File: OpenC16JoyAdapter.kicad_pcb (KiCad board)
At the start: 2 copper layers, 30.5 x 33 mm, 13 parts, among them J1 DB9 Male, P1 CONN_01X08, P2 CONN_01X02, U1 74LS244

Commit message: Refined board a bit
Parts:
- removed G***: LOGO, w_logo:Logo_copper_OSHW_6x6mm
- added P3: OSHW_LOGO_PLACEHOLDER, w_logo:Logo_copper_OSHW_6x6mm, B.Cu at (157.2, 109.0)
- C1: footprint smd_cap:c_0805 -> Capacitors_SMD:C_0805_HandSoldering
- D1: footprint LEDs:LED_0805 -> LEDs:LED_0805_HandSoldering
- P1: value CONN_01X08 -> TO_C16_MINI_DIN_8
- P2: value CONN_01X02 -> PIN5_POWER
- turned C1 to 270 degrees
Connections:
- net /DOWN renamed /c16_down
- net /FIRE renamed /c16_fire
- net /LEFT renamed /c16_left
- net /RIGHT renamed /c16_right
- net /SEL renamed /c16_select
- net /UP renamed /c16_up
- net Net-(J1-Pad1) renamed /md_up
- net Net-(J1-Pad2) renamed /md_down
- net Net-(J1-Pad3) renamed /md_left
- net Net-(J1-Pad4) renamed /md_right
- net Net-(J1-Pad6) renamed /md_b_~a
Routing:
- net GND: track 47.8 -> 56.9 mm, vias 2 -> 3
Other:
- board text added: "github.com/SukkoPera/OpenC16JoyAdapter"
- board text removed: "https://github.com/SukkoPera/"

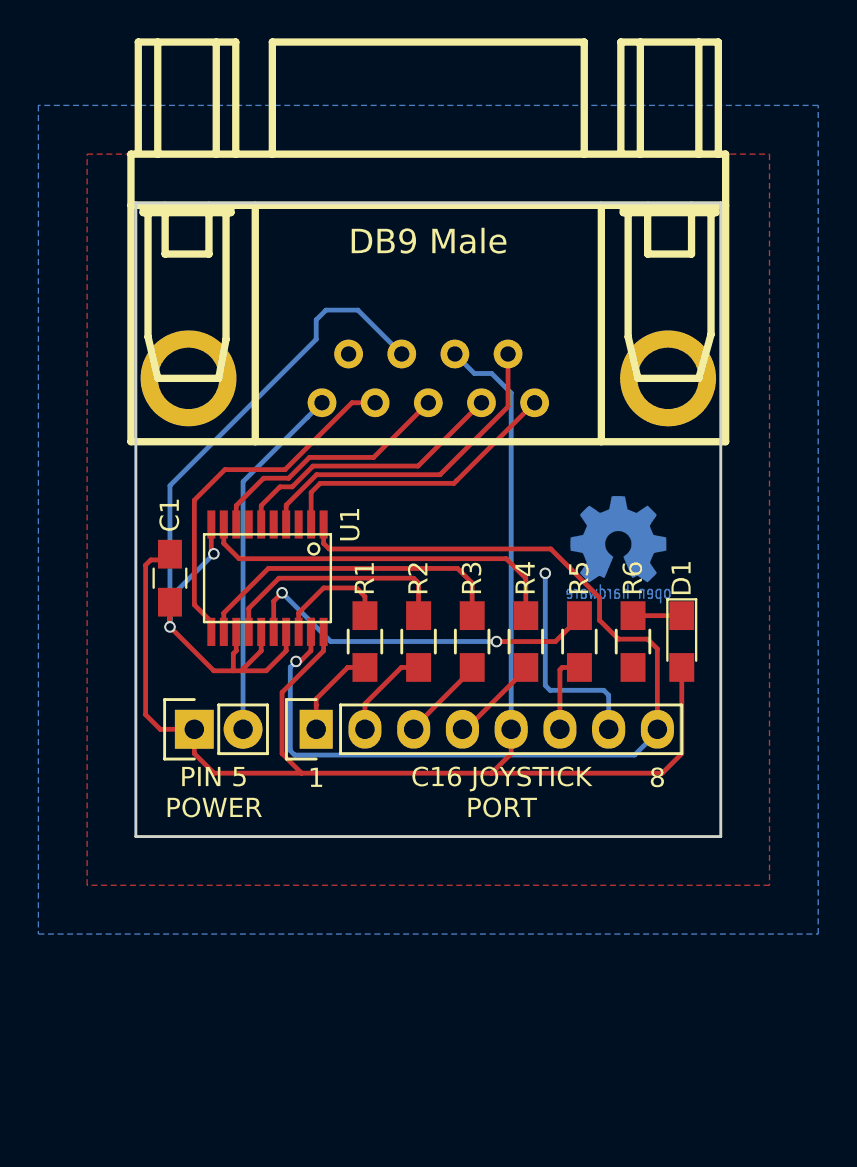
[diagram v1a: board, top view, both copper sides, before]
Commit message: Smooth lower corners, stitch ground planes, fix 3D models, add version no.
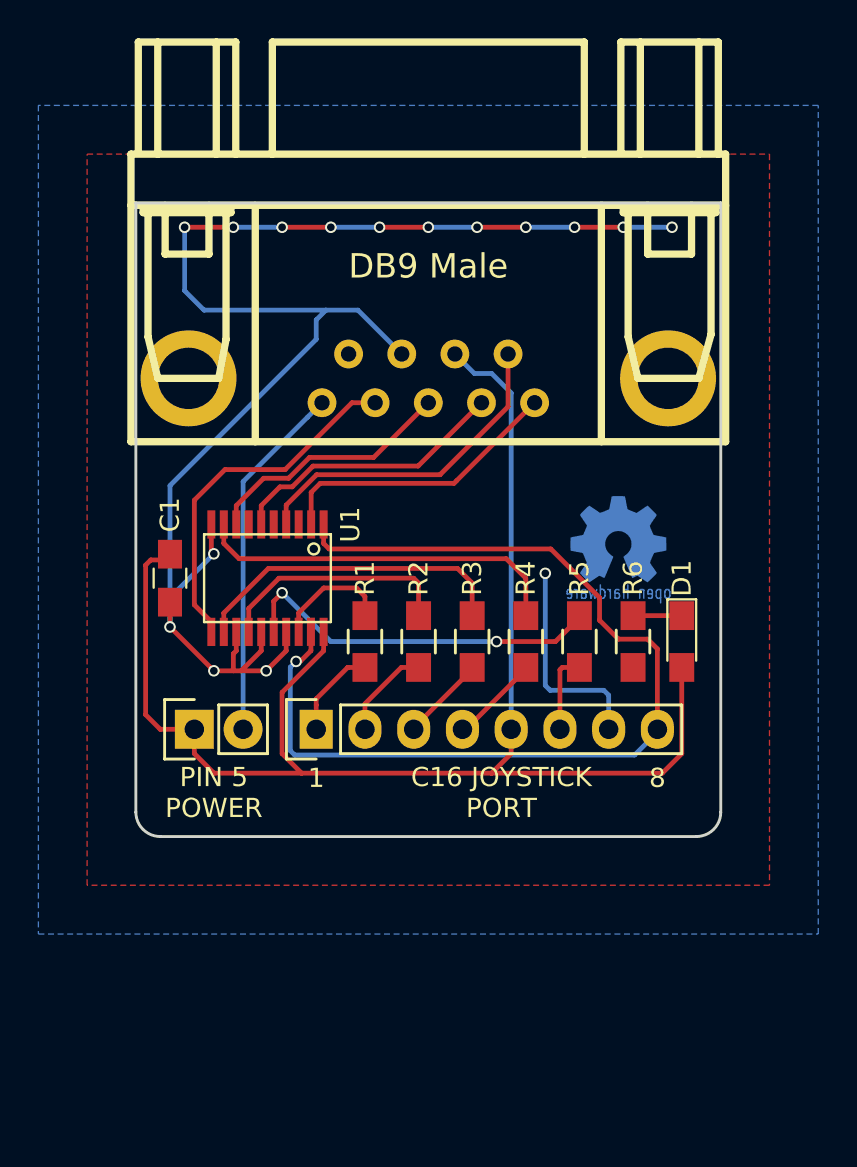
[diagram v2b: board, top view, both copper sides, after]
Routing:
- net GND: track 56.9 -> 93.4 mm, vias 3 -> 16
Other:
- outline, holes or cut-outs redrawn
- board text added: "V2"
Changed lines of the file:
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@@
 (kicad_pcb (version 4) (host pcbnew 4.0.7)
   (general
-    (links 31)
+    (links 0)
     (no_connects 0)
     (area 132.004999 91.364999 162.635001 124.535001)
     (thickness 1.6)
-    (drawings 11)
-    (tracks 159)
+    (drawings 14)
+    (tracks 185)
     (zones 0)
     (modules 13)
@@
       (effects (font (thickness 0.3048)))
     )
-    (fp_text value "DB9 Male" (at 0 0 180) (layer F.SilkS)
+    (fp_text value "DB9 Male" (at 0 -1.27 180) (layer F.SilkS)
       (effects (font (thickness 0.3048)))
     )
@@
     (pad 8 thru_hole oval (at 0 17.78 90) (size 2.032 1.7272) (drill 1.016) (layers *.Cu *.Mask)
       (net 20 /c16_select))
-    (model Pin_Headers.3dshapes/Pin_Header_Straight_1x08.wrl
-      (at (xyz 0 -0.35 0))
-      (scale (xyz 1 1 1))
-      (rotate (xyz 0 0 90))
+    (model Pin_Headers.3dshapes/Pin_Header_Straight_1x08_Pitch2.54mm.wrl
+      (at (xyz 0 0 0))
+      (scale (xyz 1 1 1))
+      (rotate (xyz 0 0 0))
     )
   )
@@
     (pad 2 thru_hole oval (at 0 2.54 90) (size 2.032 2.032) (drill 1.016) (layers *.Cu *.Mask)
       (net 8 "Net-(J1-Pad5)"))
-    (model Pin_Headers.3dshapes/Pin_Header_Straight_1x02.wrl
-      (at (xyz 0 -0.05 0))
-      (scale (xyz 1 1 1))
-      (rotate (xyz 0 0 90))
+    (model Pin_Headers.3dshapes/Pin_Header_Straight_1x02_Pitch2.54mm.wrl
+      (at (xyz 0 0 0))
+      (scale (xyz 1 1 1))
+      (rotate (xyz 0 0 0))
     )
   )
@@
       (xy -1.51384 -2.24536)) (layer B.Cu) (width 0.00254))
   )
+  (gr_text V2 (at 134.62 94.488) (layer B.SilkS)
+    (effects (font (size 1.5 1.5) (thickness 0.3)) (justify mirror))
+  )
+  (gr_arc (start 161.29 123.19) (end 162.56 123.19) (angle 90) (layer Edge.Cuts) (width 0.15))
+  (gr_arc (start 133.35 123.19) (end 133.35 124.46) (angle 90) (layer Edge.Cuts) (width 0.15))
   (gr_text github.com/SukkoPera/OpenC16JoyAdapter (at 147.32 122.174) (layer B.SilkS)
     (effects (font (size 1 0.85) (thickness 0.15)) (justify mirror))
@@
     (arrow2b (pts (xy 175.26 91.44) (xy 175.846421 92.566504)))
   )
-  (gr_line (start 132.08 124.46) (end 132.08 91.44) (layer Edge.Cuts) (width 0.15))
-  (gr_line (start 162.56 124.46) (end 132.08 124.46) (layer Edge.Cuts) (width 0.15))
-  (gr_line (start 162.56 91.44) (end 162.56 124.46) (layer Edge.Cuts) (width 0.15))
+  (gr_line (start 132.08 123.19) (end 132.08 91.44) (layer Edge.Cuts) (width 0.15))
+  (gr_line (start 161.29 124.46) (end 133.35 124.46) (layer Edge.Cuts) (width 0.15))
+  (gr_line (start 162.56 91.44) (end 162.56 123.19) (layer Edge.Cuts) (width 0.15))
   (gr_line (start 132.08 91.44) (end 162.56 91.44) (layer Edge.Cuts) (width 0.15))
   (segment (start 151.638 118.872) (end 151.638 101.346) (width 0.25) (layer B.Cu) (net 1))
@@
   (segment (start 132.8587 110.0455) (end 132.588 110.3162) (width 0.25) (layer F.Cu) (net 1))
   (segment (start 133.858 110.0455) (end 132.8587 110.0455) (width 0.25) (layer F.Cu) (net 1))
+  (segment (start 157.48 92.71) (end 160.02 92.71) (width 0.25) (layer B.Cu) (net 2))
+  (via (at 160.02 92.71) (size 0.6) (drill 0.4) (layers F.Cu B.Cu) (net 2))
+  (segment (start 154.94 92.71) (end 157.48 92.71) (width 0.25) (layer F.Cu) (net 2))
+  (via (at 157.48 92.71) (size 0.6) (drill 0.4) (layers F.Cu B.Cu) (net 2))
+  (segment (start 152.4 92.71) (end 154.94 92.71) (width 0.25) (layer B.Cu) (net 2))
+  (via (at 154.94 92.71) (size 0.6) (drill 0.4) (layers F.Cu B.Cu) (net 2))
+  (segment (start 149.86 92.71) (end 152.4 92.71) (width 0.25) (layer F.Cu) (net 2))
+  (via (at 152.4 92.71) (size 0.6) (drill 0.4) (layers F.Cu B.Cu) (net 2))
+  (segment (start 147.32 92.71) (end 149.86 92.71) (width 0.25) (layer B.Cu) (net 2))
+  (via (at 149.86 92.71) (size 0.6) (drill 0.4) (layers F.Cu B.Cu) (net 2))
+  (segment (start 144.78 92.71) (end 147.32 92.71) (width 0.25) (layer F.Cu) (net 2))
+  (via (at 147.32 92.71) (size 0.6) (drill 0.4) (layers F.Cu B.Cu) (net 2))
+  (segment (start 142.24 92.71) (end 144.78 92.71) (width 0.25) (layer B.Cu) (net 2))
+  (via (at 144.78 92.71) (size 0.6) (drill 0.4) (layers F.Cu B.Cu) (net 2))
+  (segment (start 139.7 92.71) (end 142.24 92.71) (width 0.25) (layer F.Cu) (net 2))
+  (via (at 142.24 92.71) (size 0.6) (drill 0.4) (layers F.Cu B.Cu) (net 2))
+  (segment (start 137.16 92.71) (end 139.7 92.71) (width 0.25) (layer B.Cu) (net 2))
+  (via (at 139.7 92.71) (size 0.6) (drill 0.4) (layers F.Cu B.Cu) (net 2))
+  (segment (start 134.62 92.71) (end 137.16 92.71) (width 0.25) (layer F.Cu) (net 2))
+  (via (at 137.16 92.71) (size 0.6) (drill 0.4) (layers F.Cu B.Cu) (net 2))
+  (segment (start 134.62 96.012) (end 134.62 92.71) (width 0.25) (layer B.Cu) (net 2))
+  (via (at 134.62 92.71) (size 0.6) (drill 0.4) (layers F.Cu B.Cu) (net 2))
+  (segment (start 135.636 97.028) (end 134.62 96.012) (width 0.25) (layer B.Cu) (net 2))
+  (segment (start 141.986 97.028) (end 135.636 97.028) (width 0.25) (layer B.Cu) (net 2))
+  (via (at 138.87177 115.824) (size 0.6) (drill 0.4) (layers F.Cu B.Cu) (net 2))
+  (via (at 136.144 115.824) (size 0.6) (drill 0.4) (layers F.Cu B.Cu) (net 2))
   (segment (start 145.9357 99.314) (end 143.6497 97.028) (width 0.25) (layer B.Cu) (net 2))
   (segment (start 143.6497 97.028) (end 141.986 97.028) (width 0.25) (layer B.Cu) (net 2))

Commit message: Make power tracks wider, fix bottom ground plane
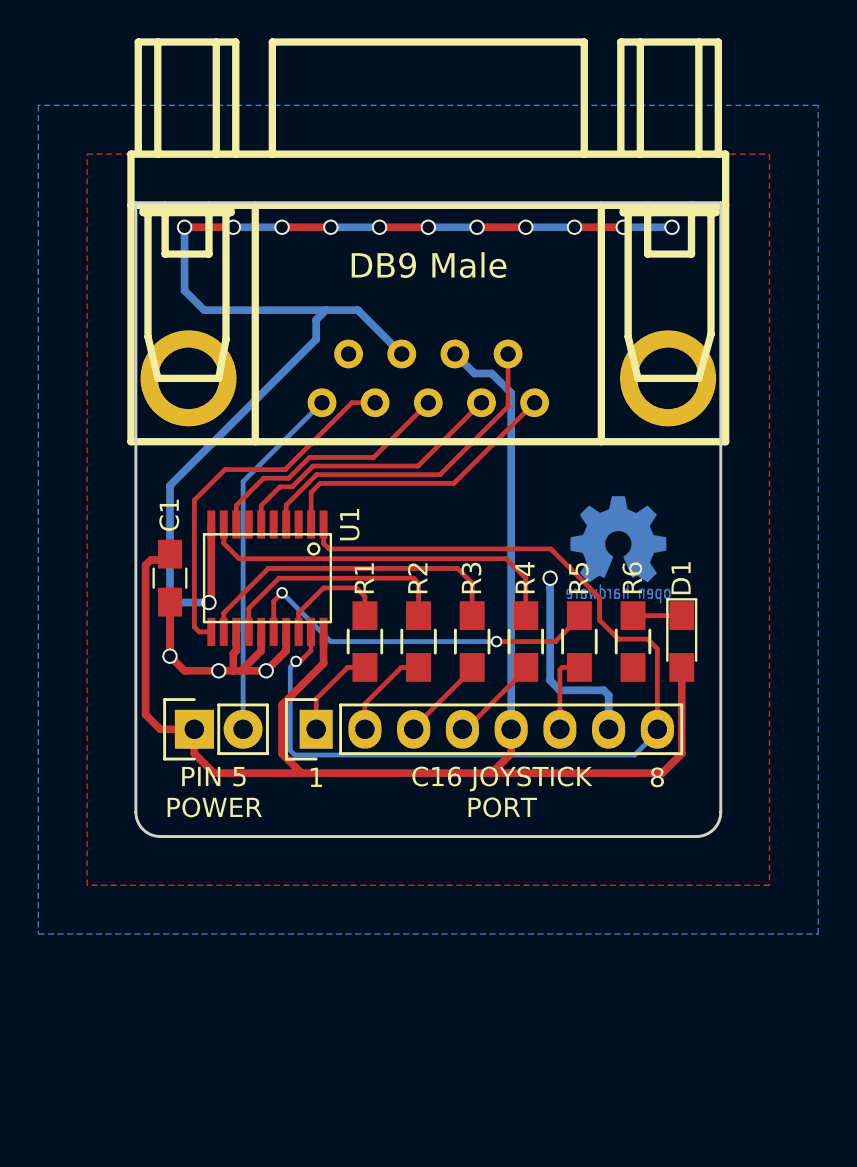
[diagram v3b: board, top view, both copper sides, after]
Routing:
- net GND: track 93.4 -> 94.7 mm
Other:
- net class Power added: clearance 0.2, trace_width 0.4, via_dia 0.8, via_drill 0.6
- rule pad_to_mask_clearance: 0.2 -> 0

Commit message: All-THT version, add pull-ups, remove led
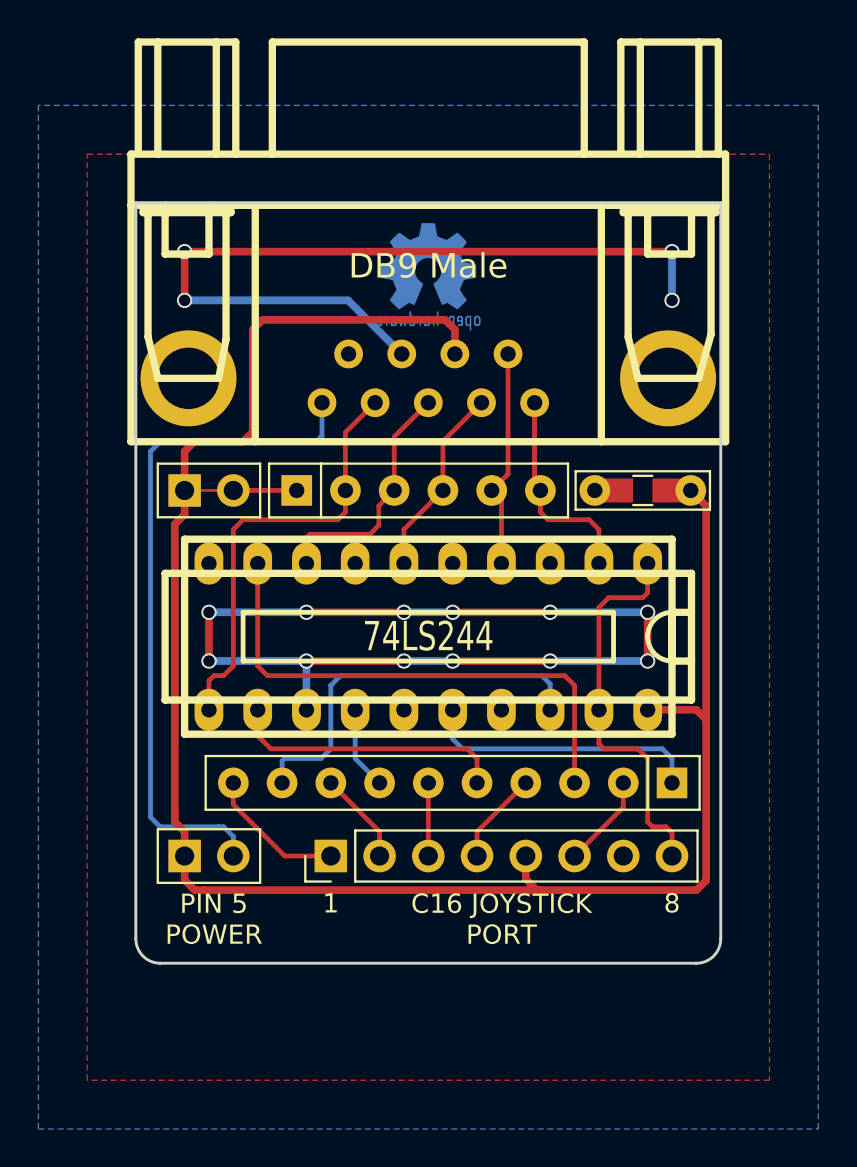
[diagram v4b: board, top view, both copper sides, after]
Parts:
- removed D1: LED, LEDs:LED_0805_HandSoldering
- removed R1, R2, R3, R4, R5: 100, Resistors_SMD:R_0805_HandSoldering
- removed R6: 680, Resistors_SMD:R_0805_HandSoldering
- added P4: PULL_UP, OpenC16JoyAdapter:Pin_Header_Straight_1x02-Cuttable, F.Cu at (134.6, 106.4)
- added RN1: 10k, Resistors_THT:R_Array_SIP6, F.Cu at (140.5, 106.4)
- added RN2: 100, Resistors_THT:R_Array_SIP10, F.Cu at (160.0, 121.7)
- C1: value C -> 100n; footprint Capacitors_SMD:C_0805_HandSoldering -> OpenC16JoyAdapter:C_0805+THT
- P1: footprint Pin_Headers:Pin_Header_Straight_1x08 -> Pin_Headers:Pin_Header_Straight_1x08_Pitch2.54mm
- P2: footprint Pin_Headers:Pin_Header_Straight_1x02 -> OpenC16JoyAdapter:Pin_Header_Straight_1x02-ModSilkS
- U1: footprint smd_dil:tssop-20 -> pth_circuits:dil_20-300_socket
- moved C1 25.1 mm to (158.5, 106.4), turned to 180 degrees
- moved P3 17.3 mm to (147.3, 94.7)
- moved U1 8.92 mm to (147.3, 114.0)
- moved P1 6.65 mm to (142.2, 125.5)
- moved P2 6.62 mm to (134.6, 125.5)
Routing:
- net /c16_select: track 52.3 -> 20.4 mm, vias 1 -> 0
- net +5V: track 77.2 -> 99.3 mm
- net Net-(J1-Pad5): track 18.7 -> 35.8 mm
- net Net-(RN2-Pad9): track 6.16 -> 20.4 mm
- net Net-(RN2-Pad7): track 12.5 -> 4.34 mm
- net Net-(RN2-Pad3): track 19.4 -> 27.3 mm
- net /md_b_~a: track 17.4 -> 11.5 mm
- net Net-(RN2-Pad1): track 19.5 -> 14.6 mm, vias 2 -> 0
- net /md_down: track 14.7 -> 10.1 mm
- net /md_right: track 19.1 -> 22.8 mm
- net Net-(P4-Pad2): track 0.00 -> 3.30 mm
- net Net-(D1-Pad1): track 2.68 -> 0.00 mm
- net Net-(RN2-Pad5): track 16.9 -> 14.5 mm
- net /c16_up: track 4.95 -> 7.32 mm
- net GND: track 94.7 -> 96.3 mm
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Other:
- board size 30.5 x 33 mm -> 30.5 x 39.6 mm

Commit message: Minor tweaks
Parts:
- RN2: footprint Resistors_THT:R_Array_SIP10 -> OpenC16JoyAdapter:R_Array_SIP10_NoPin1Mark
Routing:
- net /md_down: track 10.1 -> 10.8 mm

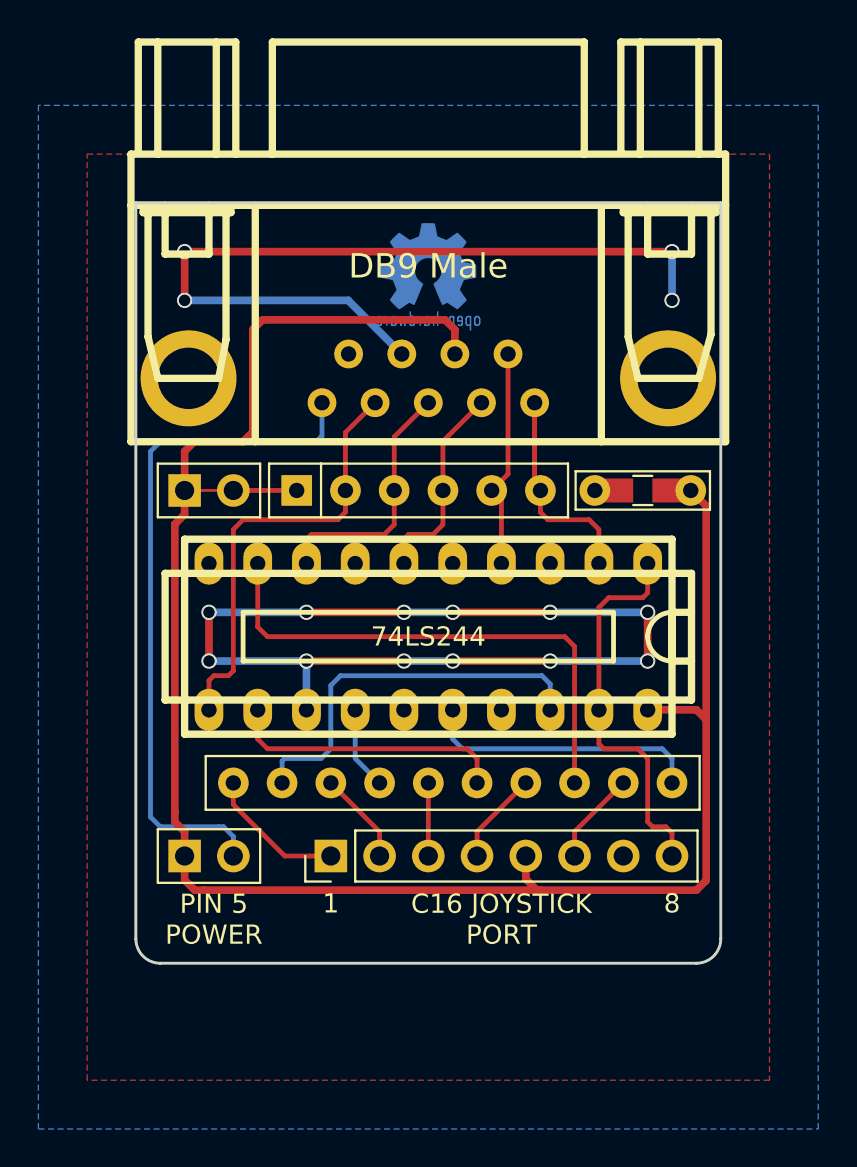
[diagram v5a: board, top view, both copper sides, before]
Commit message: Make pull-up a normal jumper and add silkscreen
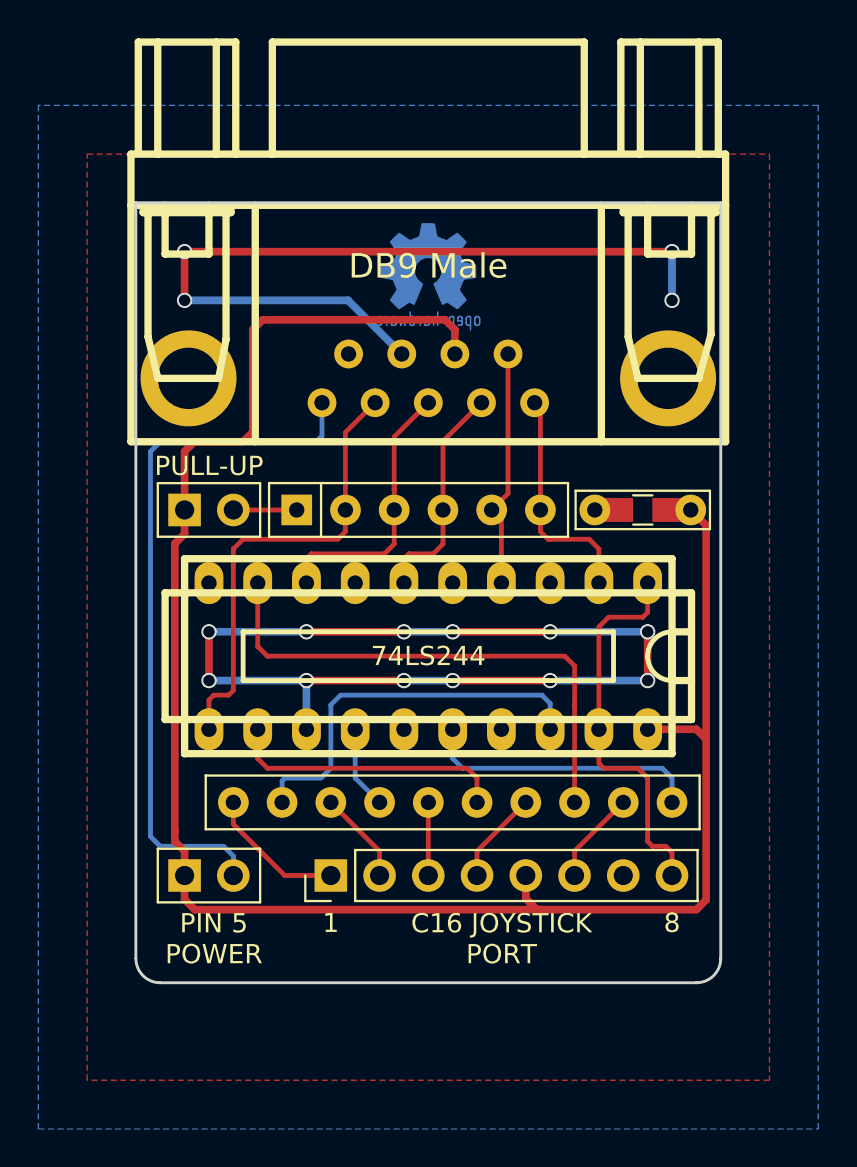
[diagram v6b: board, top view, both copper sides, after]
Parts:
- P4: footprint OpenC16JoyAdapter:Pin_Header_Straight_1x02-Cuttable -> OpenC16JoyAdapter:Pin_Header_Straight_1x02-ModSilkS
- moved P1 1.02 mm to (142.2, 126.5)
- moved P2 1.02 mm to (134.6, 126.5)
- moved RN2 1.02 mm to (160.0, 122.7)
- moved C1 1.02 mm to (158.5, 107.4)
- moved P4 1.02 mm to (134.6, 107.4)
- moved RN1 1.02 mm to (140.5, 107.4)
- moved U1 1.02 mm to (147.3, 115.1)
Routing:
- net /md_up: track 15.7 -> 12.0 mm
- net /md_left: track 13.2 -> 14.5 mm
- net +5V: track 99.3 -> 100.3 mm
- net Net-(J1-Pad5): track 35.8 -> 36.8 mm
- net /md_right: track 22.9 -> 23.9 mm
- net /md_b_~a: track 11.5 -> 12.5 mm
- net /md_down: track 10.8 -> 11.8 mm
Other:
- board size 30.5 x 39.6 mm -> 30.5 x 40.6 mm
- board text added: "PULL-UP"
